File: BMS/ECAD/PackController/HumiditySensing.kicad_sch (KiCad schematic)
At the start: 2 parts

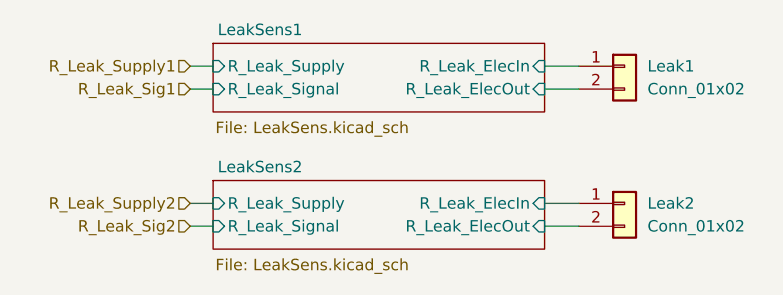
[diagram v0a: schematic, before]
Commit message: close to finish BMS master, only some footprints needed
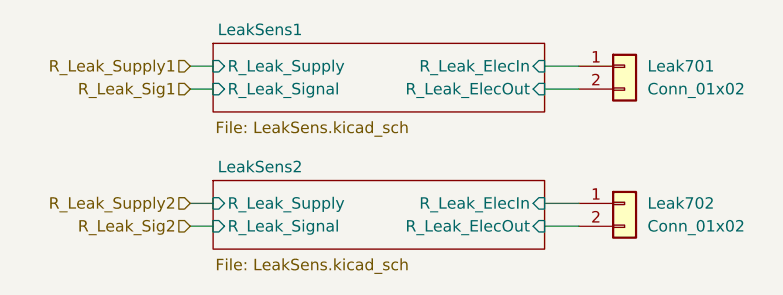
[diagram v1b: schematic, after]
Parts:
- renumbered Leak1 to Leak701, Leak2 to Leak702
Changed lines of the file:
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@@
 		(dnp no)
 		(fields_autoplaced yes)
-		(property "Reference" "Leak2"
+		(property "Reference" "Leak702"
 			(at 176.53 72.3899 0)
 			(show_name no)
@@
 			(project "Pack_Controller"
 				(path "/58a1c93e-baba-4d23-9191-955e00968735/84895c30-1551-4ee7-9bdb-3f8b53d8ebdd"
-					(reference "Leak2")
+					(reference "Leak702")
 					(unit 1)
 				)
@@
 		(dnp no)
 		(fields_autoplaced yes)
-		(property "Reference" "Leak1"
+		(property "Reference" "Leak701"
 			(at 176.53 57.1499 0)
 			(show_name no)
@@
 			(project "Pack_Controller"
 				(path "/58a1c93e-baba-4d23-9191-955e00968735/84895c30-1551-4ee7-9bdb-3f8b53d8ebdd"
-					(reference "Leak1")
+					(reference "Leak701")
 					(unit 1)
 				)

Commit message: Add several auxilary circuits to BMS Master
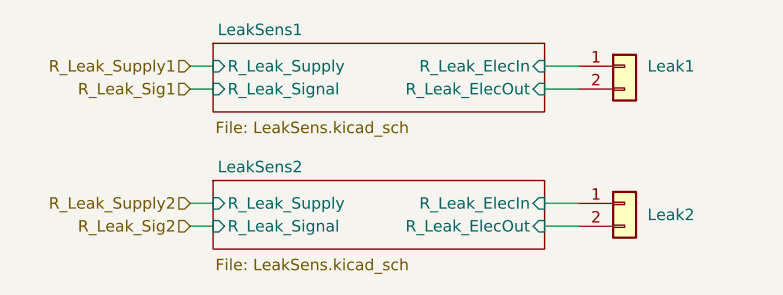
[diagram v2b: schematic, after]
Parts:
- Leak1: renamed from Leak701; footprint (none) -> Connector_Molex:Molex_Micro-Fit_3.0_43650-0215_1x02_P3.00mm_Vertical
- Leak2: renamed from Leak702; value Conn_01x02 -> (none); footprint (none) -> Connector_Molex:Molex_Micro-Fit_3.0_43650-0215_1x02_P3.00mm_Vertical
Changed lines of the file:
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@@
 		(dnp no)
 		(fields_autoplaced yes)
-		(property "Reference" "Leak702"
-			(at 176.53 72.3899 0)
+		(property "Reference" "Leak2"
+			(at 176.53 73.6599 0)
 			(show_name no)
 			(do_not_autoplace no)
@@
 			)
 		)
-		(property "Value" "Conn_01x02"
+		(property "Value" ""
 			(at 176.53 74.9299 0)
 			(show_name no)
@@
 			)
 		)
-		(property "Footprint" ""
+		(property "Footprint" "Connector_Molex:Molex_Micro-Fit_3.0_43650-0215_1x02_P3.00mm_Vertical"
 			(at 173.99 72.39 0)
 			(hide yes)
@@
 			(project "Pack_Controller"
 				(path "/58a1c93e-baba-4d23-9191-955e00968735/84895c30-1551-4ee7-9bdb-3f8b53d8ebdd"
-					(reference "Leak702")
+					(reference "Leak2")
 					(unit 1)
 				)
@@
 		(dnp no)
 		(fields_autoplaced yes)
-		(property "Reference" "Leak701"
+		(property "Reference" "Leak1"
 			(at 176.53 57.1499 0)
 			(show_name no)
@@
 		(property "Value" "Conn_01x02"
 			(at 176.53 59.6899 0)
+			(hide yes)
 			(show_name no)
 			(do_not_autoplace no)
@@
 			)
 		)
-		(property "Footprint" ""
+		(property "Footprint" "Connector_Molex:Molex_Micro-Fit_3.0_43650-0215_1x02_P3.00mm_Vertical"
 			(at 173.99 57.15 0)
 			(hide yes)
@@
 			(project "Pack_Controller"
 				(path "/58a1c93e-baba-4d23-9191-955e00968735/84895c30-1551-4ee7-9bdb-3f8b53d8ebdd"
-					(reference "Leak701")
+					(reference "Leak1")
 					(unit 1)
 				)
